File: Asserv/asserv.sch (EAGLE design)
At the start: 8 parts, among them IC1 7805TV

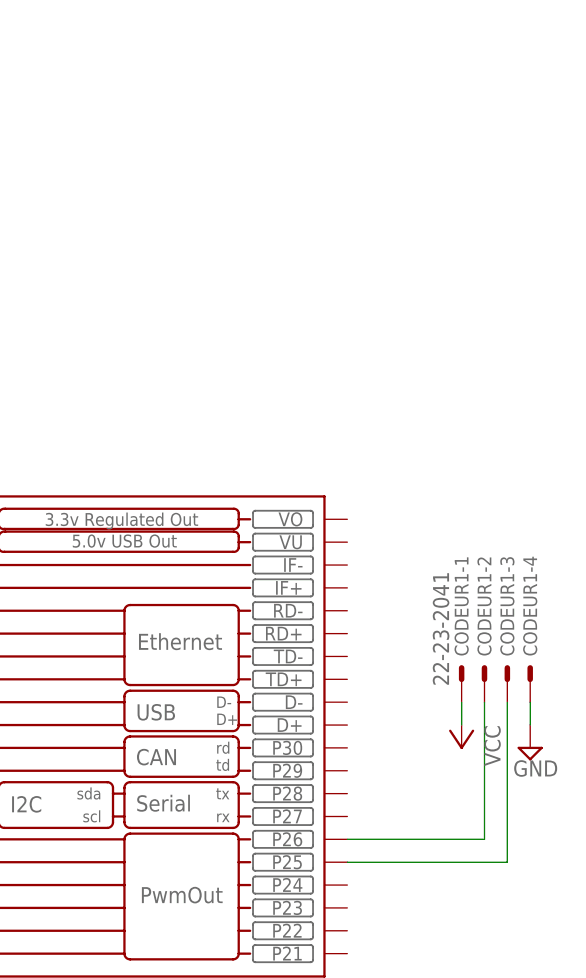
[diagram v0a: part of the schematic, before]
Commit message: ajout d'un i2c sur l'asserv et design de l'ia
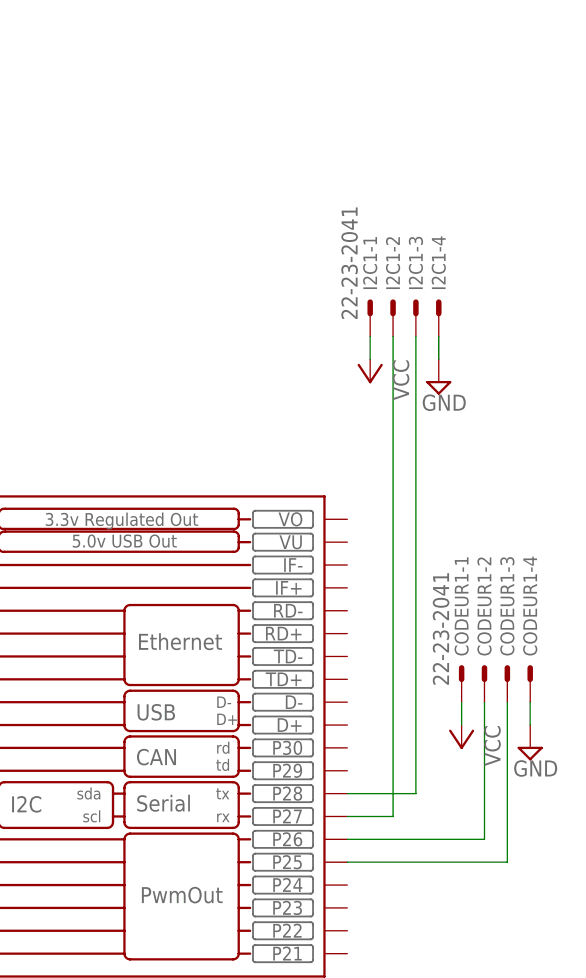
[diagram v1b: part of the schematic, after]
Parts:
- added I2C1: 22-23-2041, con-molex:22-23-2041
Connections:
- new net N$2: I2C1-2.S, KIT1.P27
- new net N$3: I2C1-3.S, KIT1.P28
- net GND: now also I2C1-4.S
- net VCC: now also I2C1-1.S
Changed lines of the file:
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@@
 <?xml version="1.0" encoding="utf-8"?>
 <!DOCTYPE eagle SYSTEM "eagle.dtd">
-<eagle version="8.2.1">
+<eagle version="8.6.3">
 <drawing>
 <settings>
 <setting alwaysvectorfont="no"/>
+<setting keepoldvectorfont="yes"/>
 <setting verticaltext="up"/>
 </settings>
@@
 <part name="P+4" library="supply1" library_urn="urn:adsk.eagle:library:371" deviceset="VCC" device=""/>
 <part name="SUPPLY5" library="supply2" library_urn="urn:adsk.eagle:library:372" deviceset="GND" device=""/>
+<part name="I2C1" library="con-molex" library_urn="urn:adsk.eagle:library:165" deviceset="22-23-2041" device=""/>
+<part name="SUPPLY6" library="supply2" library_urn="urn:adsk.eagle:library:372" deviceset="GND" device=""/>
+<part name="P+5" library="supply1" library_urn="urn:adsk.eagle:library:371" deviceset="VCC" device=""/>
 </parts>
 <sheets>
@@
 <instance part="P+4" gate="VCC" x="259.08" y="134.62" rot="R180"/>
 <instance part="SUPPLY5" gate="GND" x="147.32" y="165.1" rot="R180"/>
+<instance part="I2C1" gate="-1" x="248.92" y="182.88" rot="R90"/>
+<instance part="I2C1" gate="-2" x="251.46" y="182.88" rot="R90"/>
+<instance part="I2C1" gate="-3" x="254" y="182.88" rot="R90"/>
+<instance part="I2C1" gate="-4" x="256.54" y="182.88" rot="R90"/>
+<instance part="SUPPLY6" gate="GND" x="256.54" y="175.26"/>
+<instance part="P+5" gate="VCC" x="248.92" y="175.26" rot="R180"/>
 </instances>
 <busses>
@@
 <wire x1="147.32" y1="160.02" x2="147.32" y2="162.56" width="0.1524" layer="91"/>
 </segment>
+<segment>
+<pinref part="SUPPLY6" gate="GND" pin="GND"/>
+<pinref part="I2C1" gate="-4" pin="S"/>
+<wire x1="256.54" y1="177.8" x2="256.54" y2="180.34" width="0.1524" layer="91"/>
+</segment>
 </net>
 <net name="VCC" class="0">
@@
 <wire x1="259.08" y1="139.7" x2="259.08" y2="137.16" width="0.1524" layer="91"/>
 </segment>
+<segment>
+<pinref part="P+5" gate="VCC" pin="VCC"/>
+<pinref part="I2C1" gate="-1" pin="S"/>
+<wire x1="248.92" y1="177.8" x2="248.92" y2="180.34" width="0.1524" layer="91"/>
+</segment>
 </net>
 <net name="N$5" class="0">
@@
 <wire x1="246.38" y1="124.46" x2="261.62" y2="124.46" width="0.1524" layer="91"/>
 <wire x1="261.62" y1="124.46" x2="261.62" y2="139.7" width="0.1524" layer="91"/>
+</segment>
+</net>
+<net name="N$2" class="0">
+<segment>
+<pinref part="I2C1" gate="-2" pin="S"/>
+<wire x1="251.46" y1="180.34" x2="251.46" y2="127" width="0.1524" layer="91"/>
+<pinref part="KIT1" gate="KIT" pin="P27"/>
+<wire x1="251.46" y1="127" x2="246.38" y2="127" width="0.1524" layer="91"/>
+</segment>
+</net>
+<net name="N$3" class="0">
+<segment>
+<pinref part="I2C1" gate="-3" pin="S"/>
+<pinref part="KIT1" gate="KIT" pin="P28"/>
+<wire x1="254" y1="180.34" x2="254" y2="129.54" width="0.1524" layer="91"/>
+<wire x1="254" y1="129.54" x2="246.38" y2="129.54" width="0.1524" layer="91"/>
 </segment>
 </net>
@@
 <compatibility>
 <note version="8.2" severity="warning">
-Since Version 8.2, Eagle supports online libraries. The ids
+Since Version 8.2, EAGLE supports online libraries. The ids
 of those online libraries will not be understood (or retained)
 with this version.

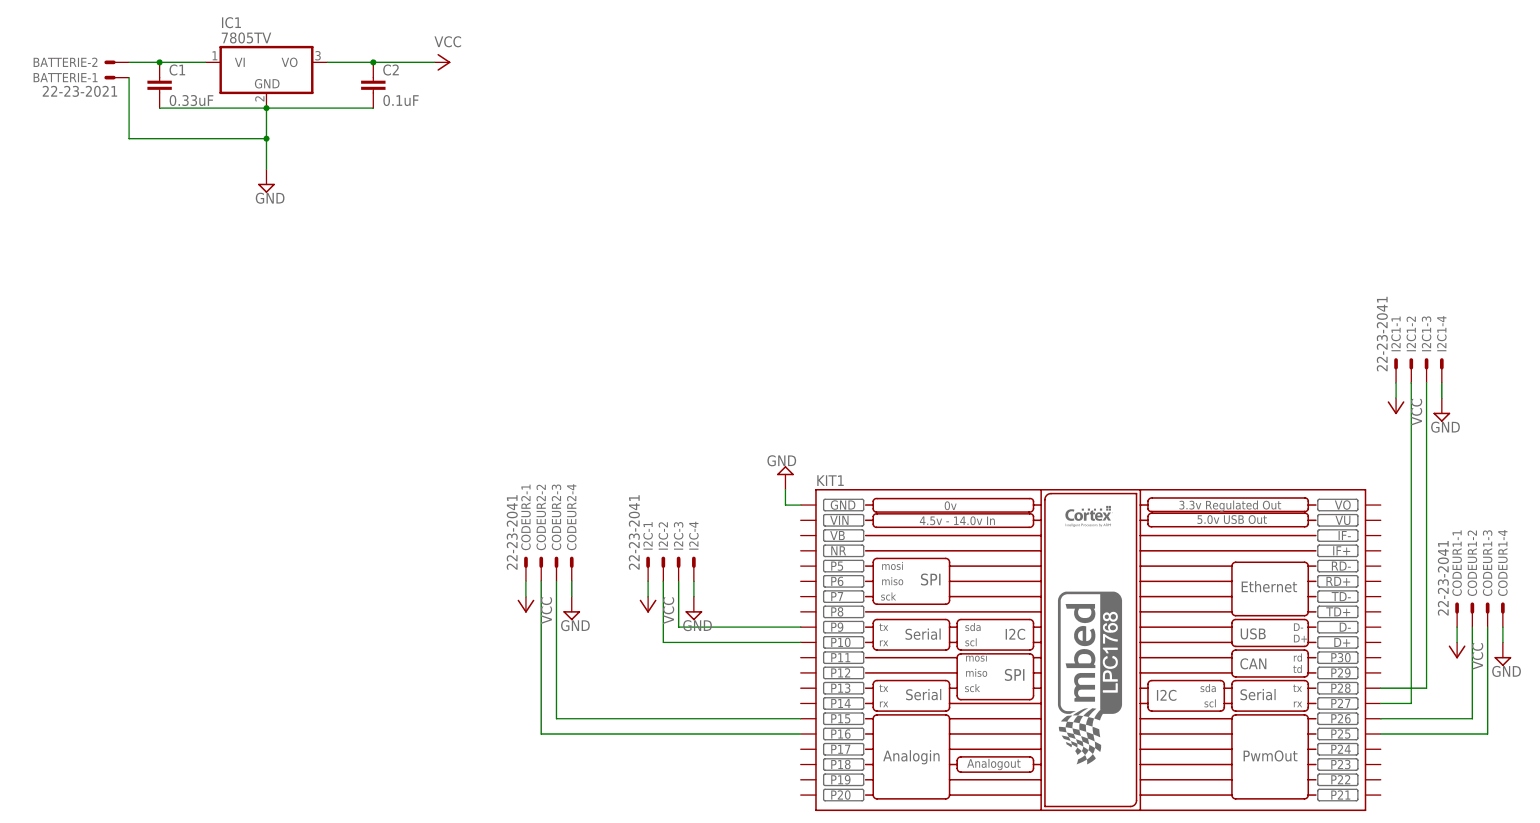
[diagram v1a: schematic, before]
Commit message: lidar + reset mbed + trou ax12
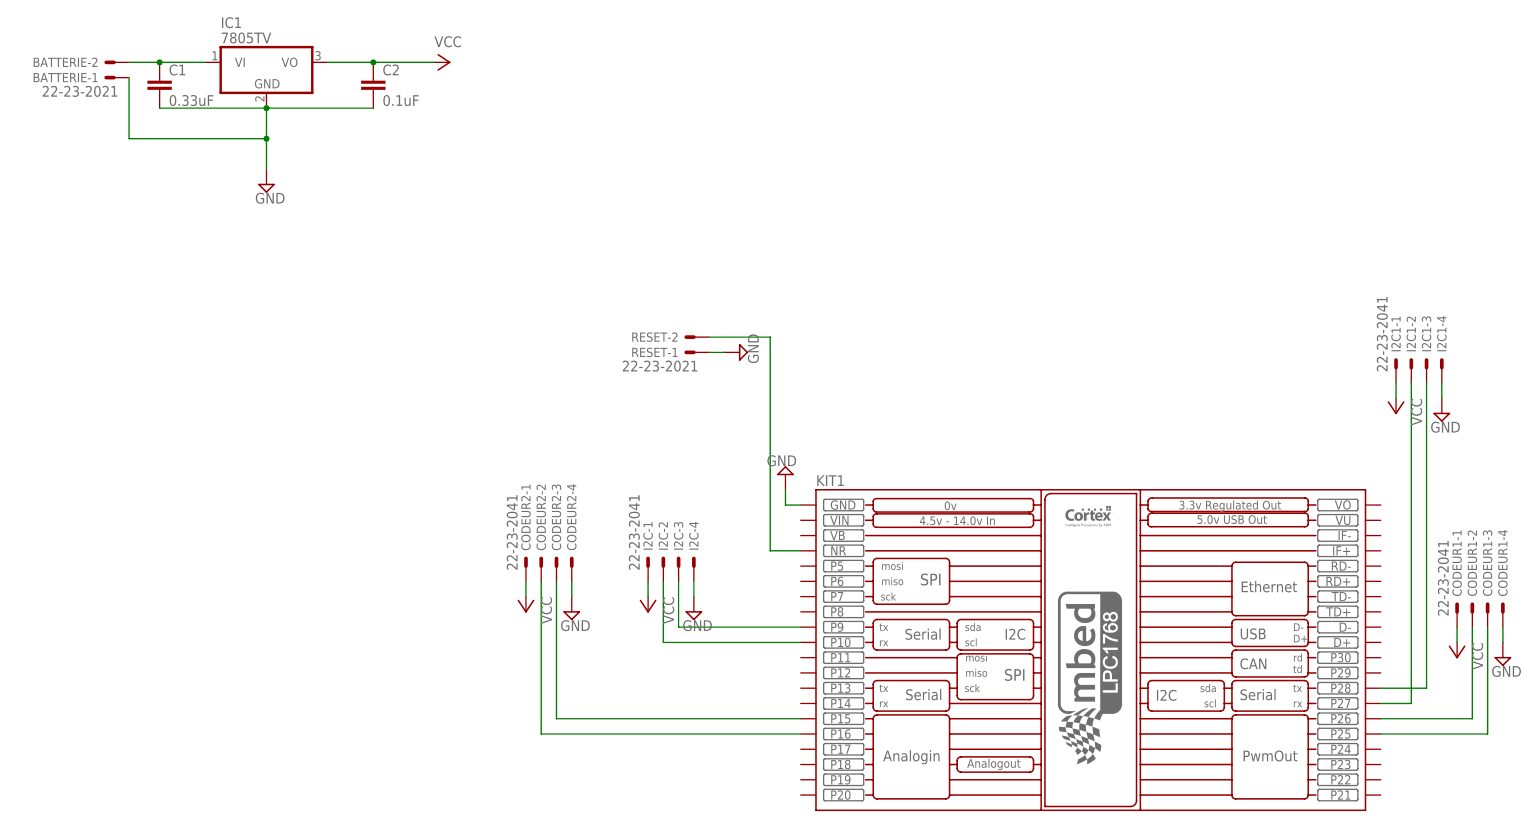
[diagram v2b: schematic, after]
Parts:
- added RESET: 22-23-2021, con-molex:22-23-2021
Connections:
- new net N$4: KIT1.NR, RESET-2.S
- net GND: now also RESET-1.S
